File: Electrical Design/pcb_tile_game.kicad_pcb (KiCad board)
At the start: 2 copper layers, 69.3 x 60 mm, 41 parts, among them J1 Conn_01x05_Pin, J2 Conn_01x05_Socket, J3 Conn_01x05_Pin, J4 Conn_01x05_Socket, J5 Conn_01x05_Pin, J6 Conn_01x05_Socket, U2 ATtiny3217-M

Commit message: updated 3D models and silkscreen
Added magnetic connector models, LED models, changed path thickness, added title, revision, and logo to silkscreen.
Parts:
- removed G***: LOGO, New Logo:byteSizedEngineeringLogo-6mm
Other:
- board text removed: "${TITLE} Rev ${REVISION}"

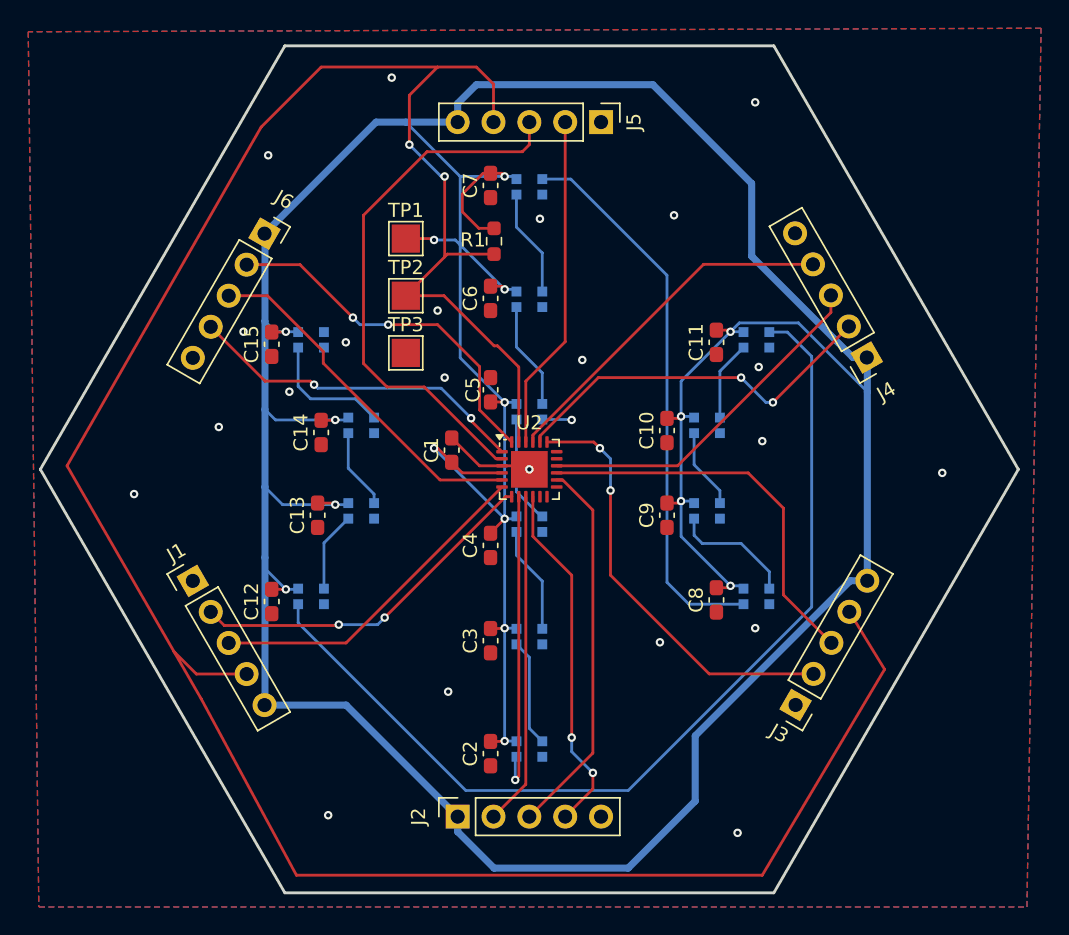
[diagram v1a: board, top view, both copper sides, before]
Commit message: Firmware, and capacitor
Added firmware folder, and added additional capacitor in parallel to C15 in schematic. Footprint still needs to be added
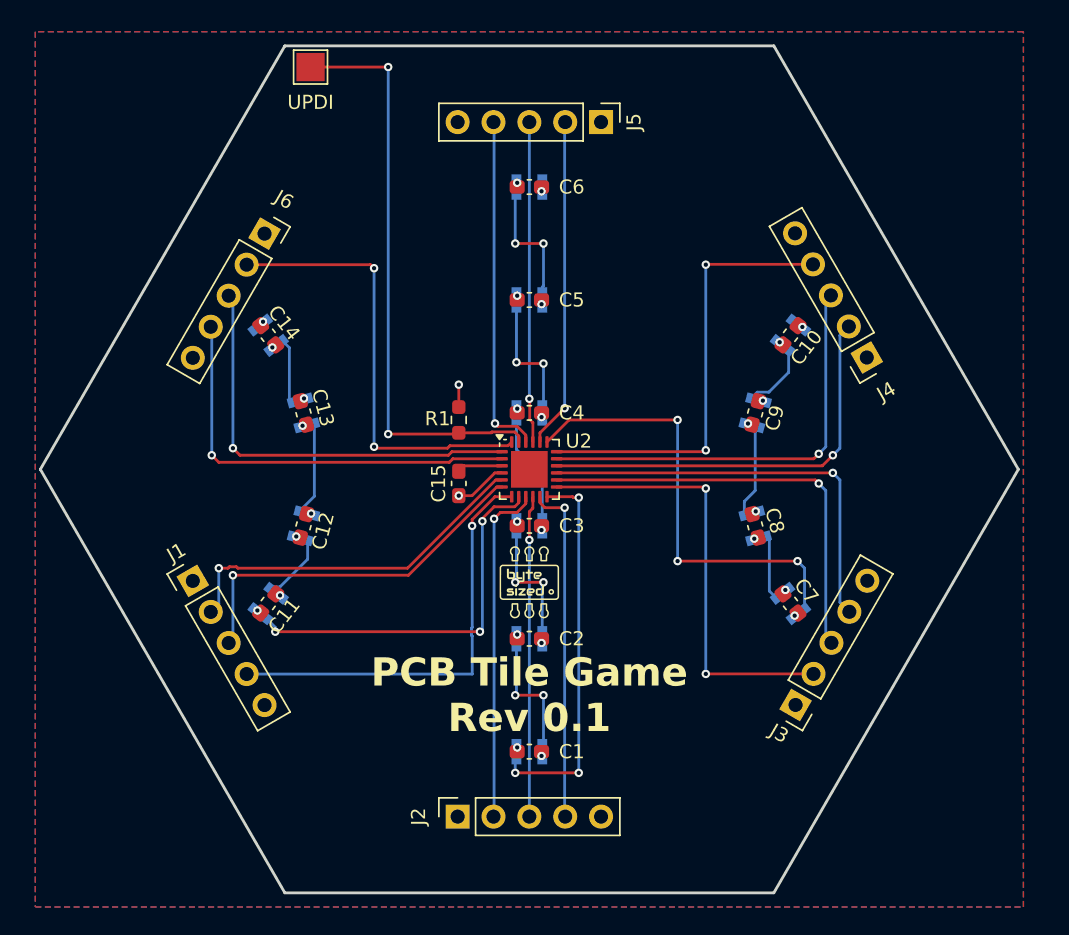
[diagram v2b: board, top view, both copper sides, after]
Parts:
- removed TP2, TP3: TestPoint, TestPoint:TestPoint_Pad_2.0x2.0mm
- added G***: LOGO, New Logo:byteSizedEngineeringLogo-6mm, F.Cu at (140.1, 88.0)
- moved TP1 13.9 mm to (124.6, 51.5)
- moved R1 12.9 mm to (135.1, 76.5)
- moved C9 6.37 mm to (156.1, 76.0), turned to -105 degrees
- moved C8 6.29 mm to (156.1, 84.0), turned to -75 degrees
- moved C10 5.27 mm to (158.6, 70.5), turned to -128 degrees
- moved C7 5.26 mm to (158.6, 89.5), turned to -52 degrees
- moved D12 4.22 mm to (124.1, 84.0), turned to -105 degrees
- moved D13 4.18 mm to (124.1, 76.0), turned to -75 degrees
- moved D8 3.58 mm to (156.1, 84.0), turned to -75 degrees
- moved D9 3.53 mm to (156.1, 76.0), turned to -105 degrees
- moved C4 3.20 mm to (140.1, 76.0), turned to 180 degrees
- moved C3 3.08 mm to (140.1, 84.0), turned to 180 degrees
- moved D11 3.08 mm to (121.6, 89.5), turned to -128 degrees
- moved D14 3.05 mm to (121.6, 70.5), turned to -52 degrees
- moved C1 2.75 mm to (140.1, 100.0), turned to 180 degrees
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- renumbered C2 to C1, C11 to C10, C12 to C11, C13 to C12, C14 to C13, C15 to C14, C1 to C15, C3 to C2, C4 to C3, C5 to C4, C6 to C5, C7 to C6, C8 to C7, C9 to C8, C10 to C9
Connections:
- net /LED_OUT_1 renamed Net-(D10-DIN)
- net /SIDE_1 renamed /DATA_J1
- net /SPARE_2a renamed /TX_J2
- net /SPARE_6a renamed /TX_J6
- D1 pad 3: /LED -> /LED_J2-J5
- D10 pad 1: Net-(D10-DOUT) -> unconnected-(D10-DOUT-Pad1)
- D11 pad 3: Net-(D10-DOUT) -> /LED_J1-J6
- D6 pad 1: Net-(D6-DOUT) -> unconnected-(D6-DOUT-Pad1)
- D7 pad 3: Net-(D6-DOUT) -> /LED_J3-J4
- J1 pad 2: /SPARE_1 -> /TX_J1
- J1 pad 4: /UPDI -> /RX_J1
- J2 pad 3: /SIDE_2 -> /DATA_J2
- J2 pad 4: /SPARE_2b -> /RX_J2
- J3 pad 2: /SPARE_3 -> /TX_J3
- J3 pad 3: /SIDE_3 -> /DATA_J3
- J3 pad 4: /UPDI -> /RX_J3
- J4 pad 2: /SPARE_4a -> /TX_J4
- J4 pad 3: /SIDE_4 -> /DATA_J4
- J4 pad 4: /SPARE_4b -> /RX_J4
- J5 pad 2: /SPARE_5 -> /TX_J5
- J5 pad 3: /SIDE_5 -> /DATA_J5
- J5 pad 4: /UPDI -> /RX_J5
- J6 pad 3: /SIDE_6 -> /DATA_J6
- J6 pad 4: /SPARE_6b -> /RX_J6
- TP1 pad 1: VCC -> /UPDI
- U2 pad 1: /SPARE_6b -> /DATA_J6
- U2 pad 10: /SPARE_2b -> /DATA_J2
- U2 pad 11: unconnected-(U2-PB5-Pad11) -> /RX_J2
- U2 pad 12: unconnected-(U2-PB4-Pad12) -> /LED_J2-J5
- U2 pad 13: unconnected-(U2-PB3-Pad13) -> /TX_J3
- U2 pad 14: /SIDE_2 -> /DATA_J3
- U2 pad 15: /SIDE_3 -> /RX_J3
- U2 pad 16: /SIDE_4 -> /TX_J4
- U2 pad 17: unconnected-(U2-PC0-Pad17) -> /DATA_J4
- U2 pad 18: unconnected-(U2-PC1-Pad18) -> /RX_J4
- U2 pad 19: /SPARE_3 -> /LED_J3-J4
- U2 pad 2: /SIDE_5 -> /RX_J6
- U2 pad 20: /SPARE_4a -> /TX_J5
- U2 pad 21: /SPARE_4b -> /DATA_J5
- U2 pad 22: /SPARE_5 -> /RX_J5
- U2 pad 5: /SIDE_6 -> /TX_J1
- U2 pad 7: /SPARE_1 -> /RX_J1
- U2 pad 8: /LED -> /LED_J1-J6
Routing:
- net VCC: track 321.7 -> 5.32 mm
- net /UPDI: track 181.2 -> 41.2 mm
- net Net-(D10-DOUT): track 69.5 -> 0.00 mm
- net Net-(D6-DOUT): track 39.5 -> 0.00 mm
- net /SIDE_5: track 38.5 -> 0.00 mm
- net /LED_J3-J4: track 0.00 -> 32.0 mm, vias 0 -> 3
- net /TX_J3: track 0.00 -> 31.4 mm, vias 0 -> 2
- net /RX_J4: track 0.00 -> 31.4 mm, vias 0 -> 2
- net /SPARE_3: track 30.5 -> 0.00 mm, vias 2 -> 0
- net /RX_J1: track 0.00 -> 30.5 mm, vias 0 -> 1
- net /RX_J6: track 0.00 -> 29.9 mm, vias 0 -> 1
- net /RX_J3: track 0.00 -> 29.9 mm, vias 0 -> 1
- net /DATA_J6: track 0.00 -> 29.9 mm, vias 0 -> 1
- net /DATA_J4: track 0.00 -> 29.8 mm, vias 0 -> 1
- net /DATA_J3: track 0.00 -> 29.8 mm, vias 0 -> 1
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- added copper zone on B.Cu, net VCC
- removed copper zone on B.Cu, net GND
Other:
- board text added: "${TITLE} Rev ${REVISION}"
- board text added: "UPDI"
